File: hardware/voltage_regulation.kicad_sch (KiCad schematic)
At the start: 33 parts, among them U4 TPS51388VABR, U5 LD39050PU33R

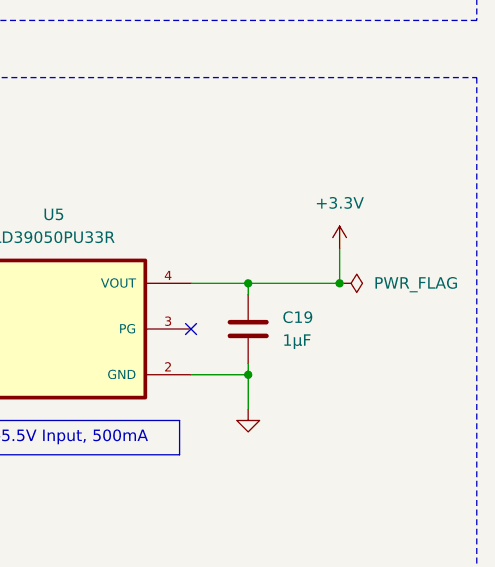
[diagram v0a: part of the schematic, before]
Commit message: Running ERC successfully
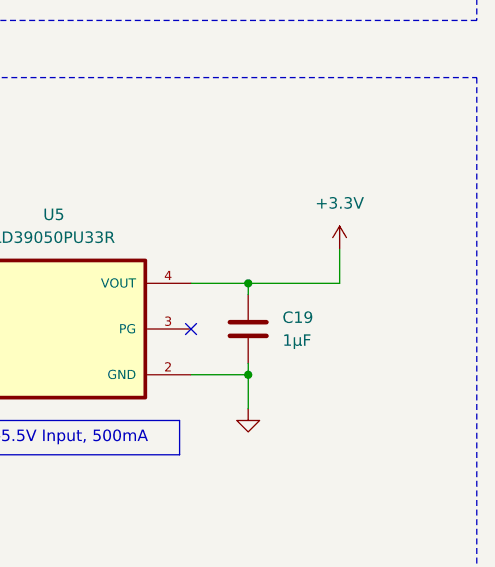
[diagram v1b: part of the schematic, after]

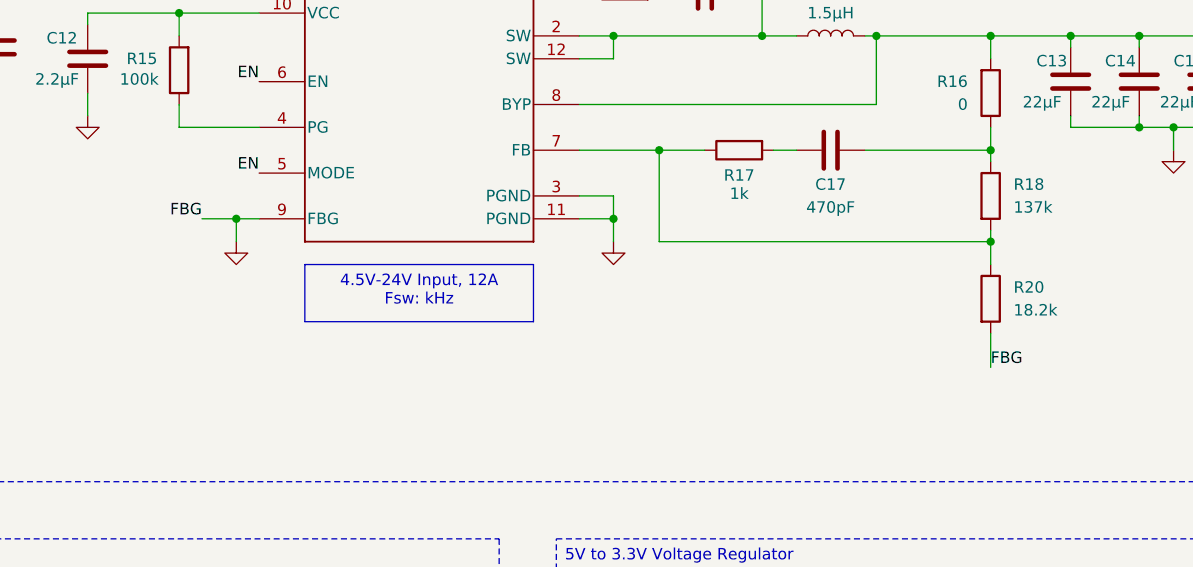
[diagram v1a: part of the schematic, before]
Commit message: Updating component placement
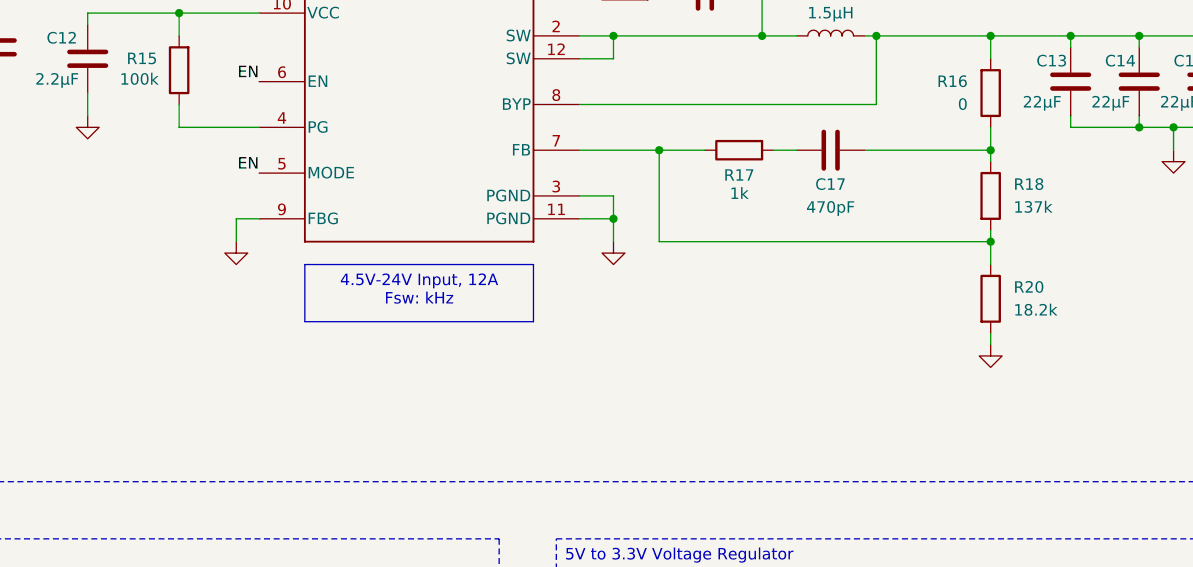
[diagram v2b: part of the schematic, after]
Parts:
- C17, C7: footprint Capacitor_SMD:C_0402_1005Metric -> Capacitor_SMD:C_0603_1608Metric
- L2: footprint Chromapi_FP:INDM6864X300N -> Chromapi_FP:IND_1040-WE-HCI_WRE
- R14: footprint Resistor_SMD:R_0402_1005Metric_Pad0.72x0.64mm_HandSolder -> Resistor_SMD:R_0603_1608Metric
- R21: footprint Resistor_SMD:R_0402_1005Metric -> Resistor_SMD:R_0603_1608Metric
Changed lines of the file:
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@@
 	)
 	(junction
-		(at 116.84 68.58)
-		(diameter 0)
-		(color 0 0 0 0)
-	)
-	(junction
 		(at 187.96 48.26)
 		(diameter 0)
@@
 	(wire
 		(pts
-			(xy 113.03 68.58) (xy 116.84 68.58)
-		)
-		(stroke
-			(width 0)
-			(type default)
-		)
-	)
-	(wire
-		(pts
 			(xy 200.66 58.42) (xy 200.66 60.96)
 		)
@@
 	(wire
 		(pts
-			(xy 200.66 81.28) (xy 200.66 85.09)
+			(xy 200.66 81.28) (xy 200.66 82.55)
 		)
 		(stroke
@@
 		)
 	)
-	(label "FBG"
-		(at 200.66 85.09 0)
-		(effects
-			(font
-				(size 1.27 1.27)
-			)
-			(justify left bottom)
-		)
-	)
 	(label "EN"
 		(at 86.36 74.93 0)
@@
 		)
 	)
-	(label "FBG"
-		(at 113.03 68.58 180)
-		(effects
-			(font
-				(size 1.27 1.27)
-			)
-			(justify right bottom)
-		)
-	)
 	(hierarchical_label "V_SYS"
 		(shape input)
@@
 			)
 		)
-		(property "Footprint" "Chromapi_FP:INDM6864X300N"
+		(property "Footprint" "Chromapi_FP:IND_1040-WE-HCI_WRE"
 			(at 182.88 48.26 0)
 			(effects
@@
 			)
 		)
-		(property "Footprint" "Resistor_SMD:R_0402_1005Metric"
+		(property "Footprint" "Resistor_SMD:R_0603_1608Metric"
 			(at 75.692 82.55 90)
 			(effects
@@
 			)
 		)
-		(property "Footprint" "Capacitor_SMD:C_0402_1005Metric"
+		(property "Footprint" "Capacitor_SMD:C_0603_1608Metric"
 			(at 179.07 61.9252 0)
 			(effects
@@
 			)
 		)
-		(property "Footprint" "Resistor_SMD:R_0402_1005Metric_Pad0.72x0.64mm_HandSolder"
+		(property "Footprint" "Resistor_SMD:R_0603_1608Metric"
 			(at 160.02 44.958 90)
 			(effects
@@
 	)
 	(symbol
+		(lib_id "power:GND")
+		(at 200.66 82.55 0)
+		(unit 1)
+		(exclude_from_sim no)
+		(in_bom yes)
+		(on_board yes)
+		(dnp no)
+		(fields_autoplaced yes)
+		(property "Reference" "#PWR0116"
+			(at 200.66 88.9 0)
+			(effects
+				(font
+					(size 1.27 1.27)
+				)
+				(hide yes)
+			)
+		)
+		(property "Value" "GND"
+			(at 200.66 87.63 0)
+			(effects
+				(font
+					(size 1.27 1.27)
+				)
+				(hide yes)
+			)
+		)
+		(property "Footprint" ""
+			(at 200.66 82.55 0)
+			(effects
+				(font
+					(size 1.27 1.27)
+				)
+				(hide yes)
+			)
+		)
+		(property "Datasheet" ""
+			(at 200.66 82.55 0)
+			(effects
+				(font
+					(size 1.27 1.27)
+				)
+				(hide yes)
+			)
+		)
+		(property "Description" "Power symbol creates a global label with name \"GND\" , ground"
+			(at 200.66 82.55 0)
+			(effects
+				(font
+					(size 1.27 1.27)
+				)
+				(hide yes)
+			)
+		)
+		(pin "1"
+		)
+		(instances
+			(project "chromapi_motherboard_v1"
+				(path "/d1a31f26-03e0-43e1-89c1-031fe31befc5/19a2634a-eca3-4c2c-b35f-9c69362f2888"
+					(reference "#PWR0116")
+					(unit 1)
+				)
+			)
+		)
+	)
+	(symbol
 		(lib_id "Device:LED")
 		(at 96.52 139.7 90)
@@
 			)
 		)
-		(property "Footprint" "Capacitor_SMD:C_0402_1005Metric"
+		(property "Footprint" "Capacitor_SMD:C_0603_1608Metric"
 			(at 165.1 44.1452 0)
 			(effects

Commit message: rm cached
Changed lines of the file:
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@@
 		)
 	)
-	(text_box "4.5V-24V Input, 12A\nFsw: kHz"
+	(text_box "4.5V-24V Input, 12A\nFsw: 600kHz"
 		(exclude_from_sim no)
 		(at 124.46 73.66 0)

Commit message: minor fix
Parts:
- U4: footprint Chromapi_FP:VAB0013A-MFG -> Chromapi_FP:TPS513885VABR
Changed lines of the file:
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@@
 			)
 		)
-		(property "Footprint" "Chromapi_FP:VAB0013A-MFG"
+		(property "Footprint" "Chromapi_FP:TPS513885VABR"
 			(at 119.38 43.18 0)
 			(hide yes)

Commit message: Updating MPN and part number
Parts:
- D5: JLCPCB Part# (none) -> C5478395; MPN 150060SS55040 -> 150060SS55040
- D6: JLCPCB Part# (none) -> C6041957
- D7: JLCPCB Part# (none) -> C6650185
- U4: JLCPCB Part# (none) -> C41935536; MPN (none) -> TPS513885VABR
- U5: JLCPCB Part# (none) -> C132827

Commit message: Updating BOM
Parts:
- C10, C8, C9: value 22µF -> 22uF; JLCPCB Part# (none) -> C69612; MPN (none) -> C3216X5R1V226M160AC
- C11, C7: JLCPCB Part# (none) -> C1591; MPN (none) -> CL10B104KB8NNNC
- C12: value 2.2µF -> 2.2uF; JLCPCB Part# (none) -> C2167658; MPN (none) -> GRM188R71A225KE15J
- C13, C14, C15, C16: value 22µF -> 22uF; JLCPCB Part# (none) -> C49326685; MPN (none) -> 0805X5R226M100NT
- C17: JLCPCB Part# (none) -> C106211; MPN (none) -> CC0603JRNPO9BN471
- C18, C19: value 1µF -> 1uF
- L2: value 1.5µH -> 1.5uH; JLCPCB Part# (none) -> C5914133; MPN (none) -> 7443552150
- R14, R16: JLCPCB Part# (none) -> C844915; MPN (none) -> CRCW06030000Z0EA
- R18: JLCPCB Part# (none) -> C137797; MPN (none) -> RC0603FR-07137KL
- R20: JLCPCB Part# (none) -> C137784; MPN (none) -> RC0603FR-0718K2L
